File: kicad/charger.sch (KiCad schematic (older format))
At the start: 1 part

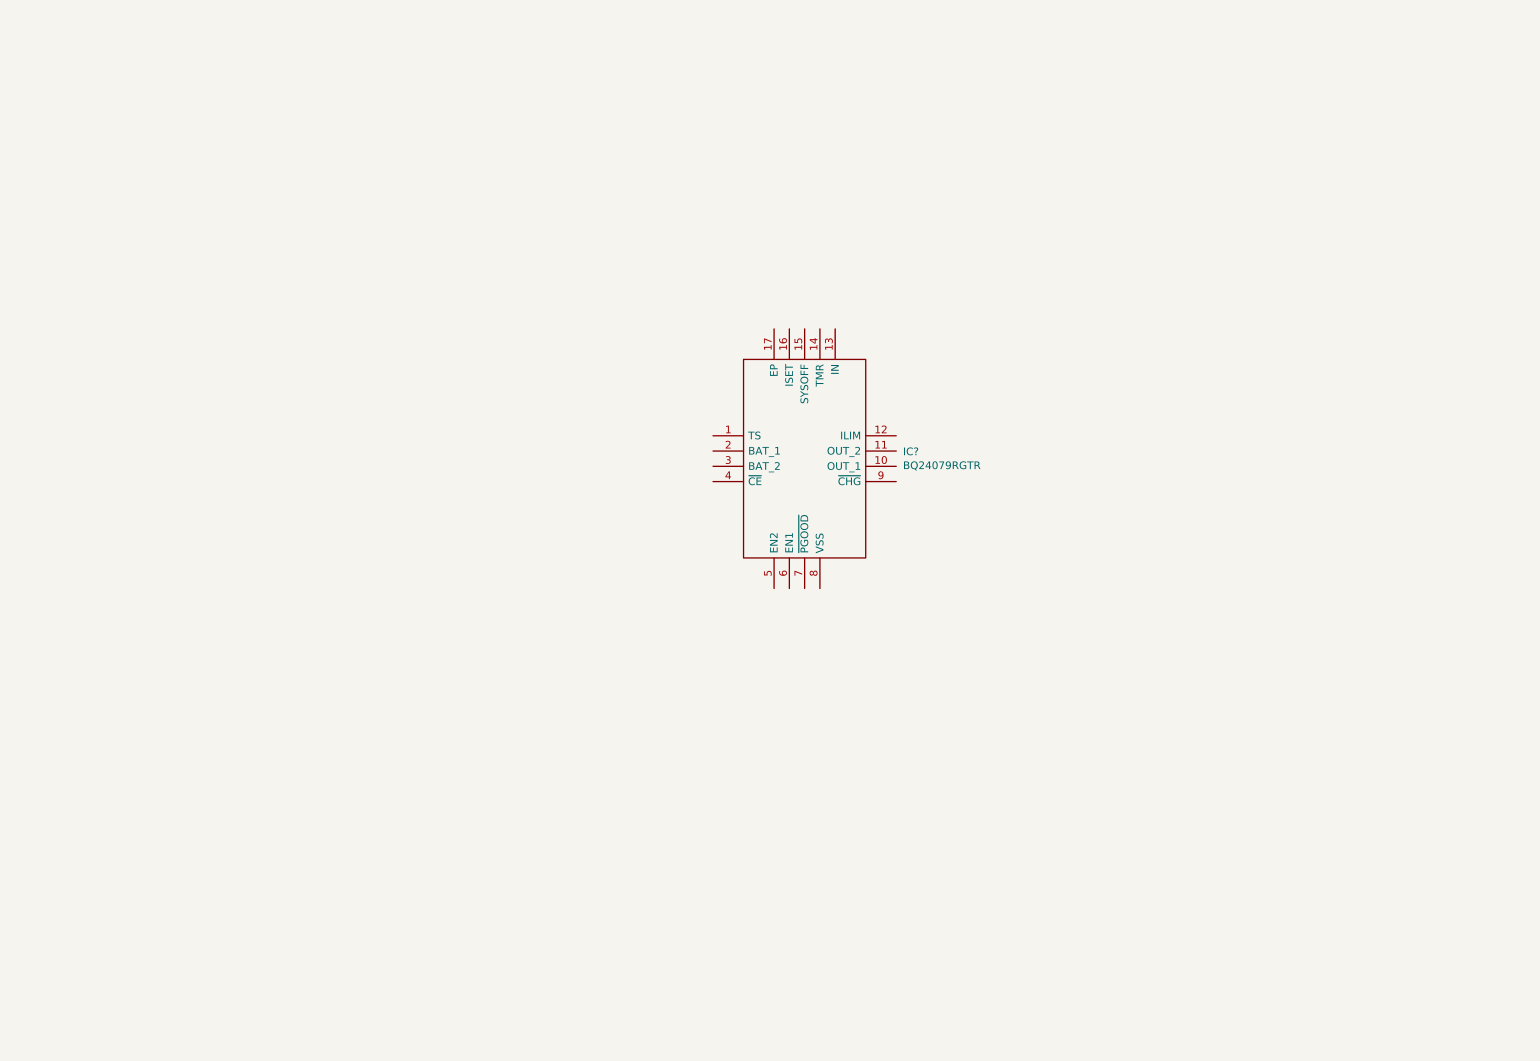
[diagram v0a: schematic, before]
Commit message: Charger initial wiring complete
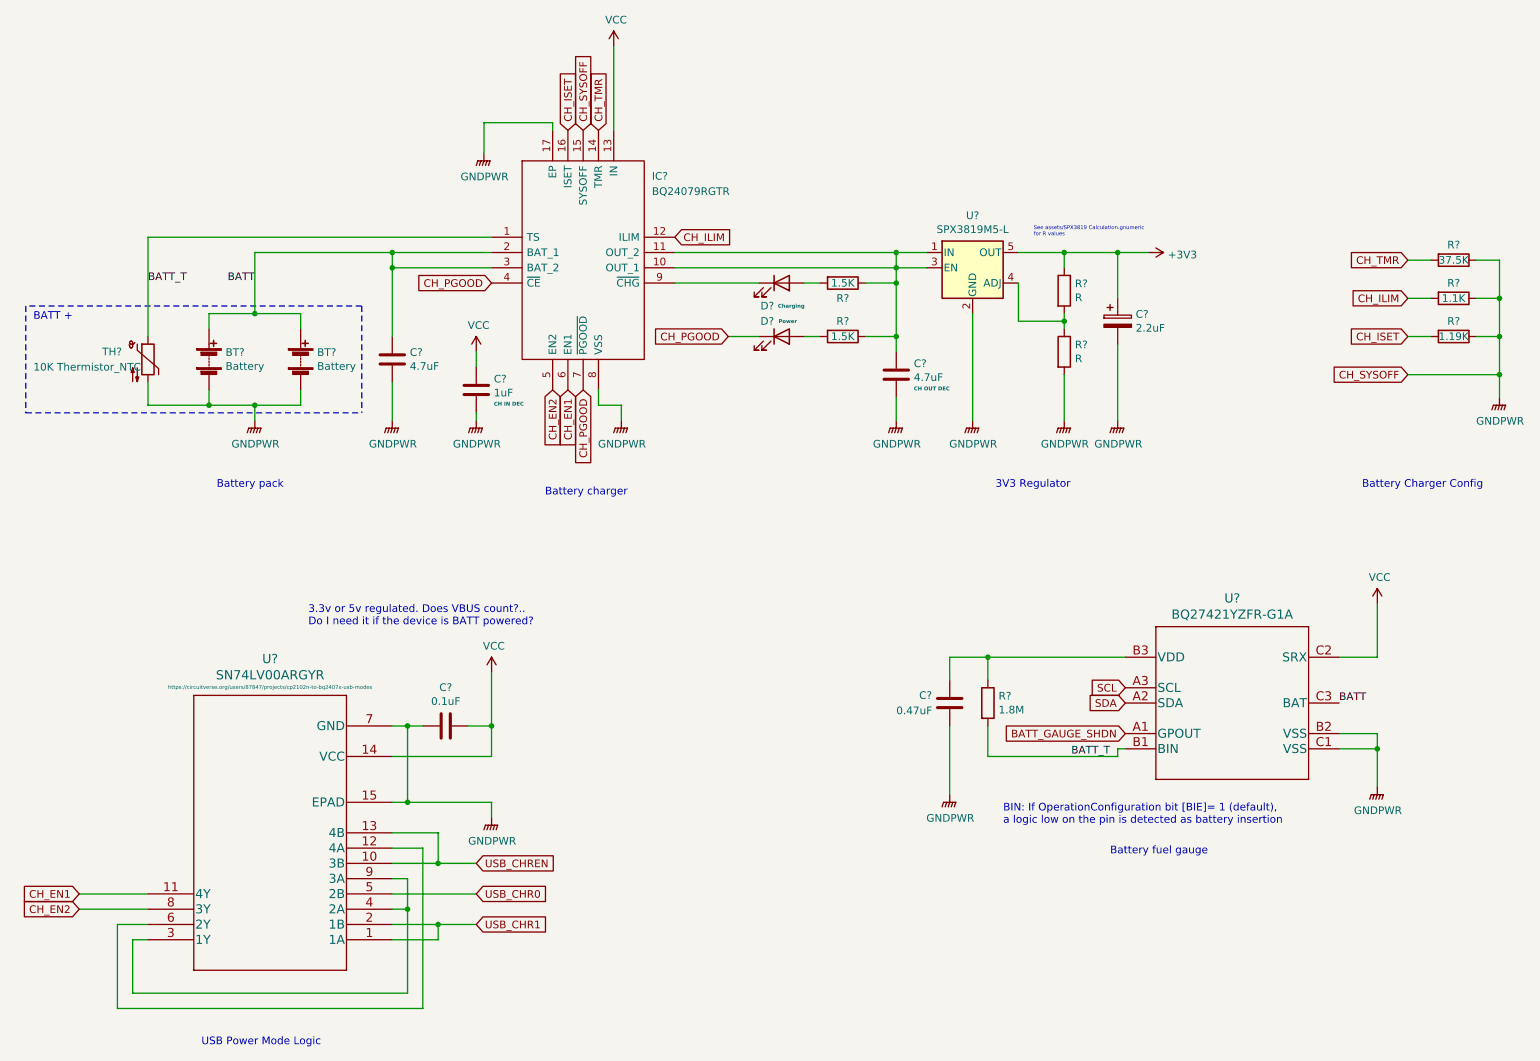
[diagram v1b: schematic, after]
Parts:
- added BT? (x2): Battery, symbol Device:Battery
- added C?: 2.2uF, symbol Device:CP
- added C?: 1uF, symbol Device:C
- added C? (x2): 4.7uF, symbol Device:C
- added C?: 0.1uF, symbol Device:C
- added C?: 0.47uF, symbol Device:C
- added D? (x2): LED, symbol Device:LED
- added R? (x2): R, symbol Device:R
- added R? (x2): 1.5K, symbol Device:R
- added R?: 1.19K, symbol Device:R
- added R?: 1.1K, symbol Device:R
- added R?: 37.5K, symbol Device:R
- added R?: 1.8M, symbol Device:R
- added TH?: 10K Thermistor_NTC, symbol Device:Thermistor_NTC
- added U?: SPX3819M5-L, Package_TO_SOT_SMD:SOT-23-5, symbol Regulator_Linear:SPX3819M5-L
- added U?: SN74LV00ARGYR, Parts:SN74LV00ARGYR, symbol Parts:SN74LV00ARGYR
- added U?: BQ27421YZFR-G1A, Parts:BQ27421YZFR-G1A, symbol Parts:BQ27421YZFR-G1A
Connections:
- net BATT_T: now reaches IC?.1 (TS)
- net BATT_T: now also R?.2, TH?.1, U?.B1 (BIN)
- net at IC?.10 (OUT_1): now also IC?.11 (OUT_2), C?.1, R?.1, R?.1, U?.1 (IN), U?.3 (EN)
- net CH_ILIM: now reaches IC?.12 (ILIM)
- net CH_ILIM: now also R?.2
- net VCC: now reaches IC?.13 (IN)
- net VCC: now also C?.1, C?.2, U?.14 (VCC), U?.C2 (SRX)
- net CH_TMR: now reaches IC?.14 (TMR)
- net CH_TMR: now also R?.2
- net GNDPWR: now reaches IC?.15 (SYSOFF)
- net GNDPWR: now also IC?.17 (EP), IC?.8 (VSS), BT?.2 (-), BT?.2 (-), C?.1, C?.2, C?.2, C?.2, C?.2, C?.2, R?.1, R?.1, R?.1, R?.2, TH?.2, U?.15 (EPAD), U?.2 (GND), U?.7 (GND), U?.B2 (VSS), U?.C1 (VSS)
- net CH_ISET: now reaches IC?.16 (ISET)
- net CH_ISET: now also R?.2
- net BATT: now reaches IC?.2 (BAT_1)
- net BATT: now also IC?.3 (BAT_2), BT?.1 (+), BT?.1 (+), C?.1, U?.C3 (BAT)
- net CH_PGOOD: now reaches IC?.4 (~CE)
- net CH_PGOOD: now also IC?.7 (~PGOOD), D?.1 (K)
- net CH_EN2: now reaches IC?.5 (EN2)
- net CH_EN2: now also U?.8 (3Y)
- net CH_EN1: now reaches IC?.6 (EN1)
- net CH_EN1: now also U?.11 (4Y)
- net at IC?.9 (~CHG): now also D?.1 (K)
- new net: R?.1, R?.2, U?.4 (ADJ)
- new net: D?.2 (A), R?.2 (x2)
- new net: U?.12 (4A), U?.6 (2Y)
- new net: U?.3 (1Y), U?.4 (2A), U?.9 (3A)
- new net: C?.1, R?.1, U?.B3 (VDD)
- new net +3V3: C?.1, R?.1, U?.5 (OUT)
- new net BATT_GAUGE_SHDN: U?.A1 (GPOUT)
- new net SCL: U?.A3 (SCL)
- new net SDA: U?.A2 (SDA)
- new net USB_CHR0: U?.5 (2B)
- new net USB_CHR1: U?.1 (1A), U?.2 (1B)
- new net USB_CHREN: U?.10 (3B), U?.13 (4B)
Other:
- note added: "3.3v or 5v regulated. Does VBUS count?.. \nDo I need it if the device is BATT powered?"
- note added: "3V3 Regulator"
- note added: "BATT +"
- note added: "BIN: If OperationConfiguration bit [BIE]= 1 (default), \na logic low on the pin is detected as battery insertion"
- note added: "Battery Charger Config"
- note added: "Battery charger"
- note added: "Battery fuel gauge"
- note added: "Battery pack"
- note added: "See assets/SPX3819 Calculation.gnumeric\nfor R values"
- note added: "USB Power Mode Logic"
- moved on the sheet: IC?

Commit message: Schematics cleanup
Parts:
- added J?: Ammeter_Jumper, Connector_PinHeader_2.54mm:PinHeader_1x02_P2.54mm_Vertical, symbol Connector_Generic:Conn_01x02
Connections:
- net +3V3: now also J?.2 (Pin_2); no longer C?.1, R?.1, U?.5 (OUT)
- new net: C?.1, J?.1 (Pin_1), R?.1, U?.5 (OUT)
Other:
- note added: "./assets/SPX3819 Calculation.gnumeric"
- note removed: "See assets/SPX3819 Calculation.gnumeric\nfor R values"
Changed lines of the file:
@@
 	2450 2750 2750 2750
 Connection ~ 2450 2750
-$Comp
-L power:GNDPWR #PWR?
-U 1 1 61092904
-P 2450 3450
-AR Path="/5F48275C/61092904" Ref="#PWR?"  Part="1"
-AR Path="/610543CF/61092904" Ref="#PWR?"  Part="1"
-F 0 "#PWR?" H 2450 3250 50  0001 C CNN
-F 1 "GNDPWR" H 2454 3296 50  0000 C CNN
-F 2 "" H 2450 3400 50  0001 C CNN
-F 3 "" H 2450 3400 50  0001 C CNN
-	1    2450 3450
-	1    0    0    -1
-$EndComp
 Wire Wire Line
 	2150 3350 2450 3350
@@
 	1    0    0    -1
 $EndComp
-Text GLabel 4600 3250 3    50   Input ~ 0
-CH_PGOOD
-Text GLabel 5550 2900 0    50   Input ~ 0
-CH_PGOOD
 $Comp
 L Device:R R?
@@
 	1    0    0    -1
 $EndComp
-Text GLabel 4700 1550 1    50   Input ~ 0
-CH_TMR
-Text GLabel 4600 1550 1    50   Input ~ 0
-CH_SYSOFF
-Text GLabel 4500 1550 1    50   Input ~ 0
-CH_ISET
-Text GLabel 4400 3250 3    50   Input ~ 0
-CH_EN2
-Text GLabel 4500 3250 3    50   Input ~ 0
-CH_EN1
 $Comp
 L power:GNDPWR #PWR?
@@
 Wire Wire Line
 	3950 1500 3950 1700
-Text GLabel 10000 2400 0    50   Input ~ 0
-CH_TMR
-Text GLabel 10000 3150 0    50   Input ~ 0
-CH_SYSOFF
-Text GLabel 10000 2900 0    50   Input ~ 0
-CH_ISET
-Text GLabel 1300 6650 0    50   Input ~ 0
-CH_EN2
-Text GLabel 1300 6550 0    50   Input ~ 0
-CH_EN1
 $Comp
 L Device:R R?
@@
 Wire Wire Line
 	10600 3150 10600 3300
-Text GLabel 5200 2250 2    50   Input ~ 0
-CH_ILIM
-Text GLabel 10000 2650 0    50   Input ~ 0
-CH_ILIM
 Wire Wire Line
 	4700 3250 4700 3350
@@
 Wire Wire Line
 	4000 5100 4000 5450
-Text GLabel 3900 6750 2    50   Input ~ 0
-USB_CHR1
-Text GLabel 3900 6550 2    50   Input ~ 0
-USB_CHR0
-Text GLabel 3900 6350 2    50   Input ~ 0
-USB_CHREN
 Wire Wire Line
 	3450 5950 4000 5950
@@
 Wire Wire Line
 	1300 6550 1750 6550
-Text GLabel 4000 2550 0    50   Input ~ 0
-CH_PGOOD
 Wire Notes Line
 	3150 2700 950  2700
@@
 $EndComp
 $Comp
-L power:+3V3 #PWR?
-U 1 1 61071C7A
-P 8300 2350
-AR Path="/5F48275C/61071C7A" Ref="#PWR?"  Part="1"
-AR Path="/610543CF/61071C7A" Ref="#PWR?"  Part="1"
-F 0 "#PWR?" H 8300 2200 50  0001 C CNN
-F 1 "+3V3" V 8315 2478 50  0000 L CNN
-F 2 "" H 8300 2350 50  0001 C CNN
-F 3 "" H 8300 2350 50  0001 C CNN
-	1    8300 2350
-	0    1    1    0
-$EndComp
-$Comp
 L Device:R R?
 U 1 1 61071C80
@@
 	7750 2350 8100 2350
 Connection ~ 7750 2350
-Connection ~ 8100 2350
-Wire Wire Line
-	8100 2350 8300 2350
 Wire Wire Line
 	8100 2350 8100 2650
-Text Notes 7550 2250 0    25   ~ 0
-See assets/SPX3819 Calculation.gnumeric\nfor R values
+Text Notes 7500 2300 0    25   ~ 0
+./assets/SPX3819 Calculation.gnumeric
 Wire Wire Line
 	5200 2350 6650 2350
@@
 	1    0    0    -1
 $EndComp
-Text GLabel 8150 5300 0    50   Input ~ 0
-SDA
-Text GLabel 8150 5200 0    50   Input ~ 0
-SCL
 Text Label 2450 2550 2    50   ~ 0
 BATT
 Text Label 9550 5300 0    50   ~ 0
 BATT
-Text GLabel 8150 5500 0    50   Input ~ 0
-BATT_GAUGE_SHDN
 $Comp
 L Device:C C?
@@
 Text Notes 9700 3900 0    50   ~ 0
 Battery Charger Config
+Text Label 4500 1550 1    50   ~ 0
+CH_ISET
+Text Label 4600 1550 1    50   ~ 0
+CH_SYSOFF
+Text Label 4700 1550 1    50   ~ 0
+CH_TMR
+Text Label 4500 3250 3    50   ~ 0
+CH_EN1
+Text Label 4400 3250 3    50   ~ 0
+CH_EN2
+Text Label 4600 3250 3    50   ~ 0
+CH_PGOOD
+Text Label 5200 2250 0    50   ~ 0
+CH_ILIM
+Text Label 4000 2550 2    50   ~ 0
+CH_PGOOD
+Text Label 5550 2900 2    50   ~ 0
+CH_PGOOD
+Text Label 10000 2900 2    50   ~ 0
+CH_ISET
+Text Label 10000 3150 2    50   ~ 0
+CH_SYSOFF
+Text Label 10000 2400 2    50   ~ 0
+CH_TMR
+Text Label 10000 2650 2    50   ~ 0
+CH_ILIM
+Text Label 1300 6550 2    50   ~ 0
+CH_EN1
+Text Label 1300 6650 2    50   ~ 0
+CH_EN2
+Text HLabel 8150 5200 0    50   Input ~ 0
+SCL
+Text HLabel 8150 5300 0    50   BiDi ~ 0
+SDA
+Text HLabel 8150 5500 0    50   Input ~ 0
+BATT_GAUGE_SHDN
+Text HLabel 3900 6350 2    50   Input ~ 0
+USB_CHREN
+Text HLabel 3900 6550 2    50   Input ~ 0
+USB_CHR0
+Text HLabel 3900 6750 2    50   Input ~ 0
+USB_CHR1
+$Comp
+L power:PWR_FLAG #FLG?
+U 1 1 6170A4CF
+P 8750 2300
+F 0 "#FLG?" H 8750 2375 50  0001 C CNN
+F 1 "PWR_FLAG" H 8750 2500 50  0000 C CNN
+F 2 "" H 8750 2300 50  0001 C CNN
+F 3 "~" H 8750 2300 50  0001 C CNN
+	1    8750 2300
+	1    0    0    -1
+$EndComp
+$Comp
+L power:+3V3 #PWR?
+U 1 1 61745A48
+P 8800 2350
+F 0 "#PWR?" H 8800 2200 50  0001 C CNN
+F 1 "+3V3" V 8815 2478 50  0000 L CNN
+F 2 "" H 8800 2350 50  0001 C CNN
+F 3 "" H 8800 2350 50  0001 C CNN
+	1    8800 2350
+	0    1    1    0
+$EndComp
+$Comp
+L power:GNDPWR #PWR?
+U 1 1 61092904
+P 2450 3450
+AR Path="/5F48275C/61092904" Ref="#PWR?"  Part="1"
+AR Path="/610543CF/61092904" Ref="#PWR?"  Part="1"
+F 0 "#PWR?" H 2450 3250 50  0001 C CNN
+F 1 "GNDPWR" H 2454 3296 50  0000 C CNN
+F 2 "" H 2450 3400 50  0001 C CNN
+F 3 "" H 2450 3400 50  0001 C CNN
+	1    2450 3450
+	1    0    0    -1
+$EndComp
+$Comp
+L Connector_Generic:Conn_01x02 J?
+U 1 1 61852947
+P 8350 2150
+AR Path="/5F48275C/61852947" Ref="J?"  Part="1"
+AR Path="/610543CF/61852947" Ref="J?"  Part="1"
+F 0 "J?" V 8600 2150 50  0000 R CNN
+F 1 "Ammeter_Jumper" V 8500 2400 50  0000 R CNN
+F 2 "Connector_PinHeader_2.54mm:PinHeader_1x02_P2.54mm_Vertical" H 8350 2150 50  0001 C CNN
+F 3 "~" H 8350 2150 50  0001 C CNN
+	1    8350 2150
+	0    -1   -1   0
+$EndComp
+Wire Wire Line
+	8350 2350 8100 2350
+Connection ~ 8100 2350
+Wire Wire Line
+	8450 2350 8750 2350
+Wire Wire Line
+	8750 2300 8750 2350
+Connection ~ 8750 2350
+Wire Wire Line
+	8750 2350 8800 2350
 $EndSCHEMATC

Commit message: Comitting yesterday's leftovers
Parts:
- added C21: 1uF, symbol Device:C
- added R34: 10k, symbol Device:R
- C19: renamed from C?; Note (none) -> Short Traces VDD VSS
- gave numbers to parts that had none: 23
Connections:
- net BATT: now also C21.1
- net CH_PGOOD: now also R34.1
- net GNDPWR: now also R35.1, C21.2; no longer U8.15 (EPAD)
- net at C19.1, U7.B3 (VDD): no longer R35.1
- new net nCH_PGOOD: R34.2
- no-connect marks 0 -> 1
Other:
- moved on the sheet: C19

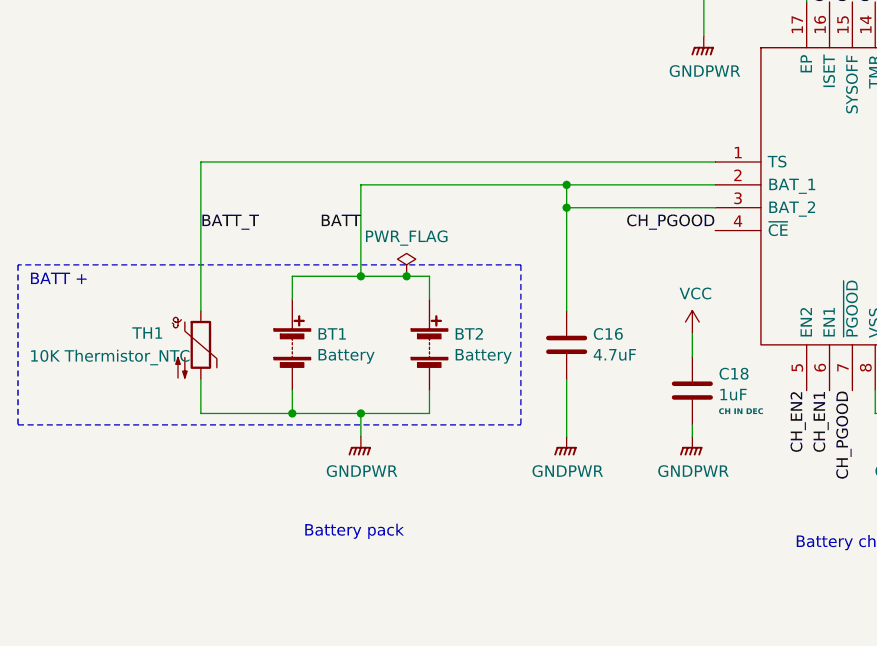
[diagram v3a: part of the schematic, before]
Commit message: Relabeled and completed ERC
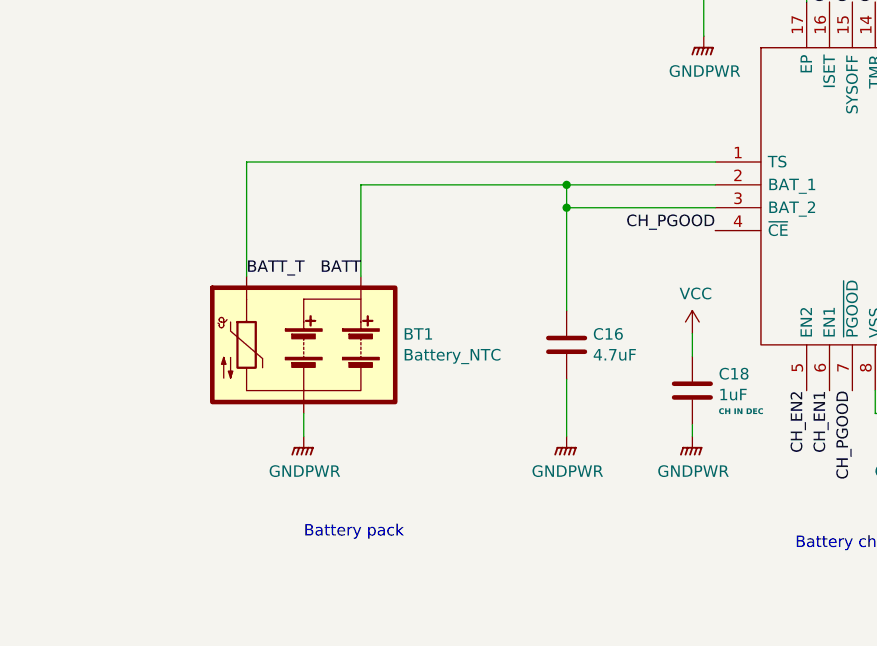
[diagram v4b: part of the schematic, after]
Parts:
- removed BT1, BT2: Battery, symbol Device:Battery
- removed TH1: 10K Thermistor_NTC, symbol Device:Thermistor_NTC
- added BT1: Battery_NTC, Connector_JST:JST_EH_B3B-EH-A_1x03_P2.50mm_Vertical, symbol Parts:Battery_NTC
- C15, C16, C17, C18, C19, C20, C21: footprint (none) -> Capacitor_SMD:C_1206_3216Metric
- D10, D9: footprint (none) -> LED_SMD:LED_0603_1608Metric
- R27, R28, R29, R30, R31, R32, R33, R34, R35: footprint (none) -> Resistor_SMD:R_0805_2012Metric
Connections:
- net BATT: now also BT1.3 (+)
- net BATT_T: now also BT1.2 (TH_NTC)
- net GNDPWR: now also BT1.1 (-)
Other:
- note removed: "BATT +"
